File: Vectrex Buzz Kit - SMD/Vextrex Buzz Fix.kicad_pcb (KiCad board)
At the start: 2 copper layers, 19.8 x 37.1 mm, 11 parts, among them U1 TL082

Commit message: 1.1
added a tiny but of solder mask keepout in an attempt to make this board look right for jlcpcb
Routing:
- net GND: vias 5 -> 0
- net (no net): vias 0 -> 5
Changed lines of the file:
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@@
     (links 14)
     (no_connects 1)
-    (area 139.192 85.852 159.512001 125.027)
+    (area 139.370999 86.030999 159.333001 123.265001)
     (thickness 1.6)
-    (drawings 9)
+    (drawings 10)
     (tracks 38)
     (zones 0)
@@
       (drillshape 0)
       (scaleselection 1)
-      (outputdirectory gerbers/))
+      (outputdirectory gerbers/1.1/))
   )
   (net 0 "")
@@
       (net 2 GND))
   )
+  (gr_line (start 140.589 122.809) (end 144.145 122.809) (angle 90) (layer B.Mask) (width 0.2))
   (gr_text v1.0 (at 139.954 121.666) (layer B.Cu)
     (effects (font (size 1.5 1.5) (thickness 0.3)) (justify right mirror))
@@
     (effects (font (size 1.5 1.5) (thickness 0.3)) (justify left mirror))
   )
+  (via (at 145.796 97.536) (size 0.6) (drill 0.4) (layers F.Cu B.Cu) (net 0))
+  (via (at 141.224 101.346) (size 0.6) (drill 0.4) (layers F.Cu B.Cu) (net 0))
+  (via (at 141.478 113.03) (size 0.6) (drill 0.4) (layers F.Cu B.Cu) (net 0))
+  (via (at 149.606 111.76) (size 0.6) (drill 0.4) (layers F.Cu B.Cu) (net 0))
+  (via (at 156.972 111.252) (size 0.6) (drill 0.4) (layers F.Cu B.Cu) (net 0))
   (segment (start 147.34 99.314) (end 145.288 99.314) (width 0.25) (layer F.Cu) (net 1))
   (segment (start 145.288 99.314) (end 142.494 96.52) (width 0.25) (layer F.Cu) (net 1))
@@
   (segment (start 146.685 102.96) (end 146.685 99.969) (width 0.25) (layer F.Cu) (net 1))
   (segment (start 146.685 99.969) (end 147.34 99.314) (width 0.25) (layer F.Cu) (net 1))
-  (via (at 145.796 97.536) (size 0.6) (drill 0.4) (layers F.Cu B.Cu) (net 2))
-  (via (at 141.224 101.346) (size 0.6) (drill 0.4) (layers F.Cu B.Cu) (net 2))
-  (via (at 141.478 113.03) (size 0.6) (drill 0.4) (layers F.Cu B.Cu) (net 2))
-  (via (at 149.606 111.76) (size 0.6) (drill 0.4) (layers F.Cu B.Cu) (net 2))
-  (via (at 156.972 111.252) (size 0.6) (drill 0.4) (layers F.Cu B.Cu) (net 2))
   (segment (start 149.84 99.314) (end 149.606 99.314) (width 0.25) (layer F.Cu) (net 2))
   (segment (start 153.69 102.108) (end 153.69 99.334) (width 0.25) (layer F.Cu) (net 3))

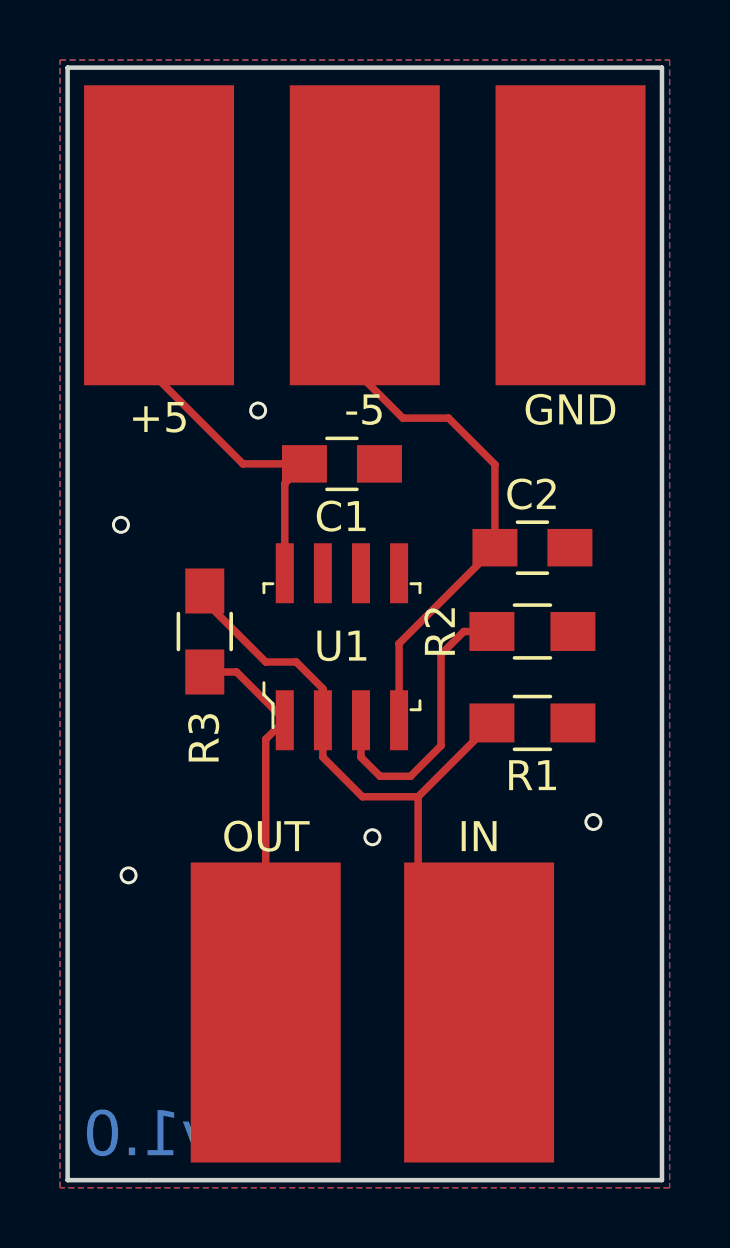
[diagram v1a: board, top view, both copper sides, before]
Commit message: Fixed Unintentional Antenna
Thanks to mobiusstriptech for the fix, applied to both SMD and THT versions.
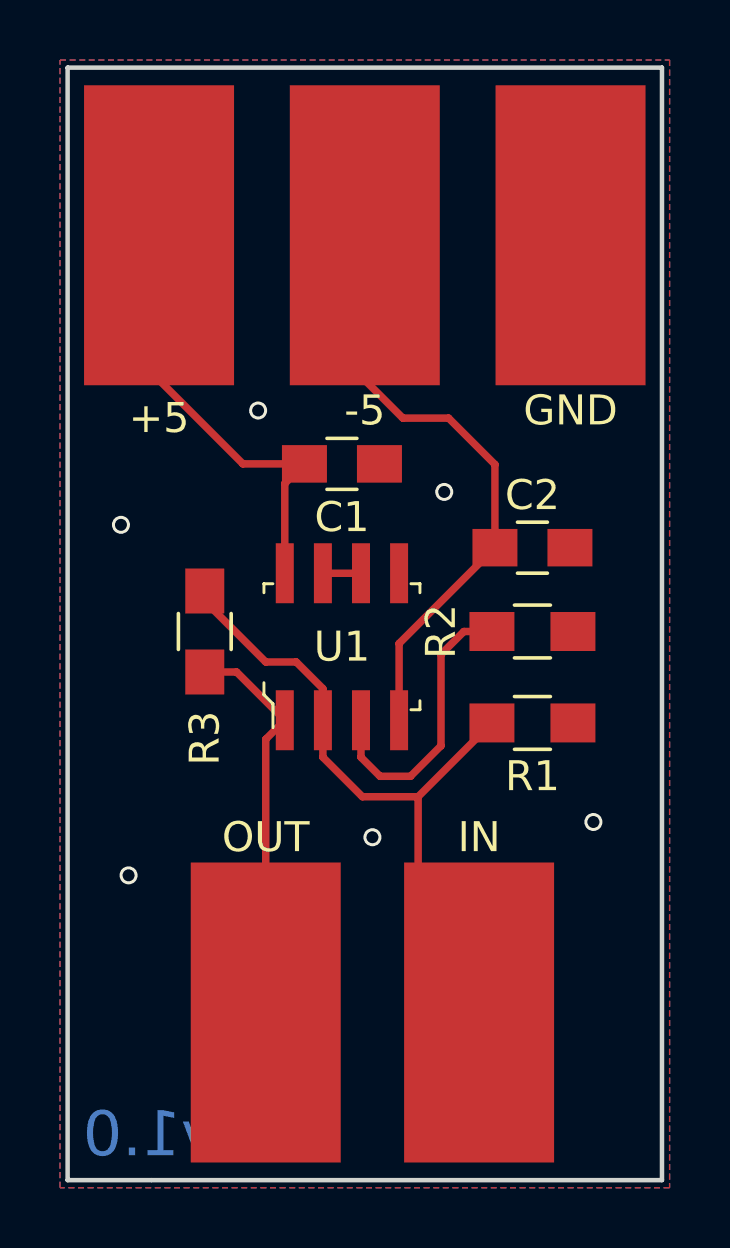
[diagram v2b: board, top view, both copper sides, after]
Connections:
- U1 pad 5: (no net) -> GND
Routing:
- net (no net): track 0.00 -> 1.27 mm, vias 5 -> 0
- net GND: vias 0 -> 6
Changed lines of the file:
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@@
-(kicad_pcb (version 4) (host pcbnew 4.0.7)
+(kicad_pcb (version 20171130) (host pcbnew "(5.1.5)-3")
   (general
-    (links 14)
-    (no_connects 1)
-    (area 139.370999 86.030999 159.333001 123.265001)
     (thickness 1.6)
     (drawings 10)
-    (tracks 38)
+    (tracks 40)
     (zones 0)
     (modules 11)
@@
     (zone_45_only no)
     (trace_min 0.2)
-    (segment_width 0.2)
-    (edge_width 0.15)
     (via_size 0.6)
     (via_drill 0.4)
@@
     (uvia_min_size 0.2)
     (uvia_min_drill 0.1)
+    (edge_width 0.15)
+    (segment_width 0.2)
     (pcb_text_width 0.3)
     (pcb_text_size 1.5 1.5)
@@
     (mod_text_size 1 1)
     (mod_text_width 0.15)
-    (pad_size 1.524 1.524)
-    (pad_drill 0.762)
+    (pad_size 0.6 2)
+    (pad_drill 0)
     (pad_to_mask_clearance 0.2)
     (aux_axis_origin 0 0)
     (visible_elements 7FFFFFFF)
     (pcbplotparams
-      (layerselection 0x010f0_80000001)
+      (layerselection 0x010f0_ffffffff)
       (usegerberextensions true)
+      (usegerberattributes false)
+      (usegerberadvancedattributes false)
+      (creategerberjobfile false)
       (excludeedgelayer true)
       (linewidth 0.100000)
@@
       (hpglpennumber 1)
       (hpglpenspeed 20)
-      (hpglpendiameter 15)
-      (hpglpenoverlay 2)
+      (hpglpendiameter 15.000000)
       (psnegative false)
       (psa4output false)
@@
       (drillshape 0)
       (scaleselection 1)
-      (outputdirectory gerbers/1.1/))
+      (outputdirectory "gerbers/1.2/"))
   )
   (net 0 "")
@@
     (pad 4 smd rect (at 1.905 2.45) (size 0.6 2) (layers F.Cu F.Paste F.Mask)
       (net 3 -5V))
-    (pad 5 smd rect (at 1.905 -2.45) (size 0.6 2) (layers F.Cu F.Paste F.Mask))
+    (pad 5 smd rect (at 1.905 -2.45) (size 0.6 2) (layers F.Cu F.Paste F.Mask)
+      (net 2 GND))
     (pad 6 smd rect (at 0.635 -2.45) (size 0.6 2) (layers F.Cu F.Paste F.Mask))
     (pad 7 smd rect (at -0.635 -2.45) (size 0.6 2) (layers F.Cu F.Paste F.Mask))
@@
     (effects (font (size 1.5 1.5) (thickness 0.3)) (justify left mirror))
   )
-  (via (at 145.796 97.536) (size 0.6) (drill 0.4) (layers F.Cu B.Cu) (net 0))
-  (via (at 141.224 101.346) (size 0.6) (drill 0.4) (layers F.Cu B.Cu) (net 0))
-  (via (at 141.478 113.03) (size 0.6) (drill 0.4) (layers F.Cu B.Cu) (net 0))
-  (via (at 149.606 111.76) (size 0.6) (drill 0.4) (layers F.Cu B.Cu) (net 0))
-  (via (at 156.972 111.252) (size 0.6) (drill 0.4) (layers F.Cu B.Cu) (net 0))
+  (segment (start 147.955 102.96) (end 149.225 102.96) (width 0.25) (layer F.Cu) (net 0))
+  (via (at 145.796 97.536) (size 0.6) (drill 0.4) (layers F.Cu B.Cu) (net 2))
+  (via (at 141.224 101.346) (size 0.6) (drill 0.4) (layers F.Cu B.Cu) (net 2))
+  (via (at 141.478 113.03) (size 0.6) (drill 0.4) (layers F.Cu B.Cu) (net 2))
+  (via (at 149.606 111.76) (size 0.6) (drill 0.4) (layers F.Cu B.Cu) (net 2))
+  (via (at 156.972 111.252) (size 0.6) (drill 0.4) (layers F.Cu B.Cu) (net 2))
   (segment (start 147.34 99.314) (end 145.288 99.314) (width 0.25) (layer F.Cu) (net 1))
   (segment (start 145.288 99.314) (end 142.494 96.52) (width 0.25) (layer F.Cu) (net 1))
@@
   (segment (start 146.685 99.969) (end 147.34 99.314) (width 0.25) (layer F.Cu) (net 1))
   (segment (start 149.84 99.314) (end 149.606 99.314) (width 0.25) (layer F.Cu) (net 2))
+  (via (at 152 100.25) (size 0.6) (drill 0.4) (layers F.Cu B.Cu) (net 2))
   (segment (start 153.69 102.108) (end 153.69 99.334) (width 0.25) (layer F.Cu) (net 3))
   (segment (start 150.622 97.79) (end 148.59 95.758) (width 0.25) (layer F.Cu) (net 3))
